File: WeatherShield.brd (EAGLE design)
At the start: 104.1 x 58.4 mm, 66 parts, among them J7 M023.5MM, J8 M023.5MM, Q1 BSS138, Q2 BSS138, U1 DS3231SN, U2 LT3652, U4 MPL3115A2LGA8, U5 HTU21D

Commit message: Power parts
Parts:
- removed J7, J8: M023.5MM, SparkFun-Connectors:SCREWTERMINAL-3.5MM-2
- removed L1: 68uH, SparkFun-Passives:CR75
- added L2: (no value), rcl:6000-XXXX-RC
- C3, C4: device SparkFun-Capacitors:EIA3528 -> FSEWeatherShield:EIA7343-20
- R21, R23, R8: device rcl:R0603 -> rcl:R0805
- U$3: value DEAN_CONNECTOR -> V_BATT
- moved R23 172.0 mm to (41.9, 67.3), turned to 180 degrees
- moved R21 164.7 mm to (41.9, 63.5), turned to 180 degrees
- moved R22 147.9 mm to (38.1, 55.9), turned to 180 degrees
- moved TP1 138.2 mm to (41.9, 49.5), turned to 180 degrees
- moved R10 126.4 mm to (41.9, 43.2), turned to 180 degrees
- moved R20 119.6 mm to (30.5, 43.2), turned to 180 degrees
- moved C9 113.4 mm to (43.2, 36.8), turned to 180 degrees
- moved U2 111.9 mm to (44.5, 30.5), turned to 180 degrees
- moved JP1 108.0 mm to (41.9, 27.9), turned to 180 degrees
- moved R8 108.0 mm to (39.4, 34.3), turned to 180 degrees
- moved JP2 106.8 mm to (45.7, 26.7), turned to 180 degrees
- moved C11 104.4 mm to (30.5, 35.6), turned to 90 degrees
- moved C2 102.9 mm to (39.4, 26.7), turned to 180 degrees
- moved R9 101.6 mm to (26.7, 33.0), turned to 270 degrees
- moved C10 100.6 mm to (36.8, 30.5), turned to 270 degrees
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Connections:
- net GND: no longer J8.2
- net N$14: no longer J7.2, J8.1
- net SENSE: now also L2.2; no longer L1.P$2
- net SFSASDF: no longer J7.1
- net SW: now also L2.1; no longer L1.P$1
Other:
- board size 104.1 x 58.4 mm -> 97.8 x 67.3 mm

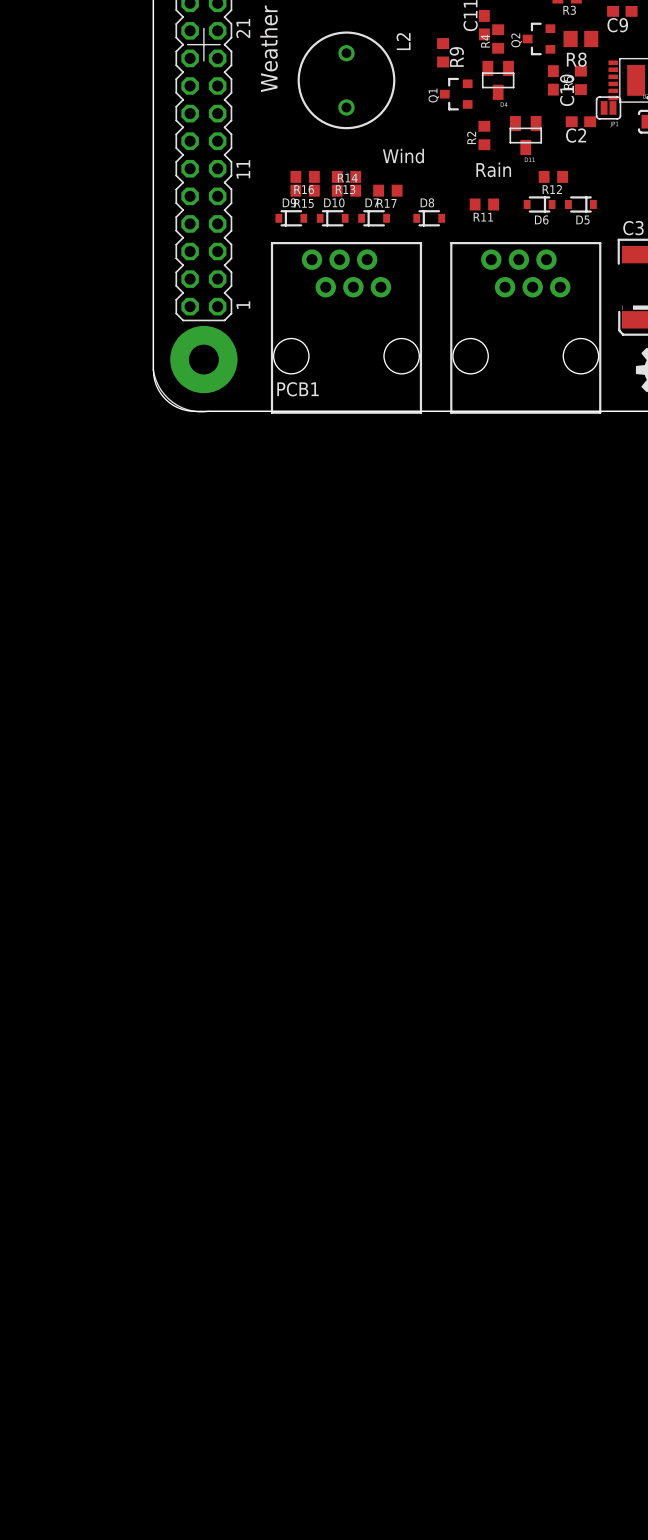
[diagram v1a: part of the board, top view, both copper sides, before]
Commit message: 5V supply done
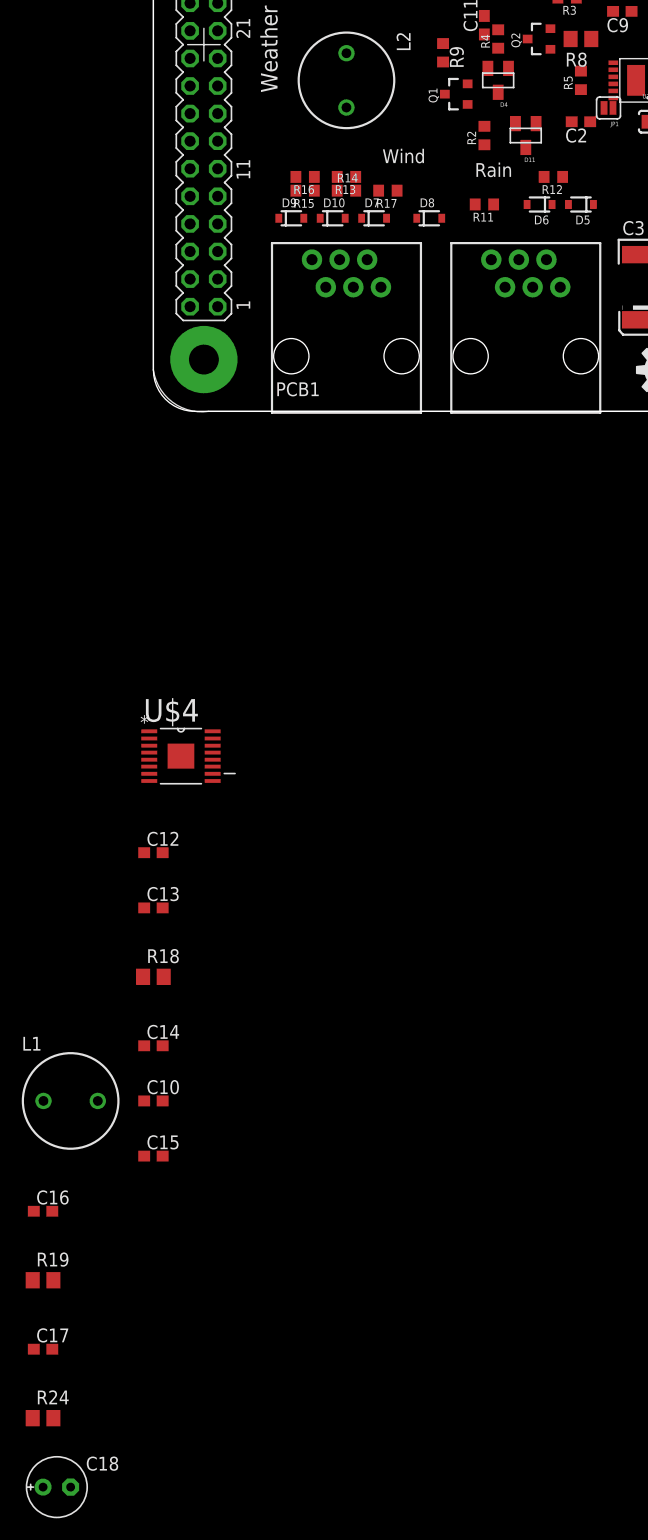
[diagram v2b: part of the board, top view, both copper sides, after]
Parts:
- added C12: 1uF, rcl:C0603
- added C13, C16: 4.7u, rcl:C0603
- added C14: 2.2uF, rcl:C0603
- added C15: 470nF, rcl:C0603
- added C17: 39pF, rcl:C0603
- added C18: 100uF, rcl:E2,5-6E
- added L1: 33uH, rcl:6000-XXXX-RC
- added R18: 0.2, rcl:R0805
- added R19: 1M, rcl:R0805
- added R24: 249k, rcl:R0805
- added U$4: LM43602, FSEWeatherShield:HTSSOP-16
- C10: value 1.0uF -> 1uF
- L2: value (none) -> 68uH
- moved C10 100.9 mm to (0.00, -63.5), turned to 0 degrees
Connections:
- new net +5V: C16.1, C17.1, C18.+, L1.2, R19.2, U$4.5
- new net N$17: C15.1, U$4.3
- new net N$21: R18.2, U$4.7
- new net N$22: C17.2, R19.1, R24.2, U$4.9
- new net N$23: C14.1, U$4.4
- new net N$24: C15.2, L1.1, U$4.1, U$4.2
- net GND: now also C12.2, C13.2, C14.2, C16.2, C18.-, R18.1, R24.1, U$4.10, U$4.15, U$4.16, U$4.17, U$4.6
- net V_BATT: now also C12.1, C13.1, U$4.12, U$4.13, U$4.14

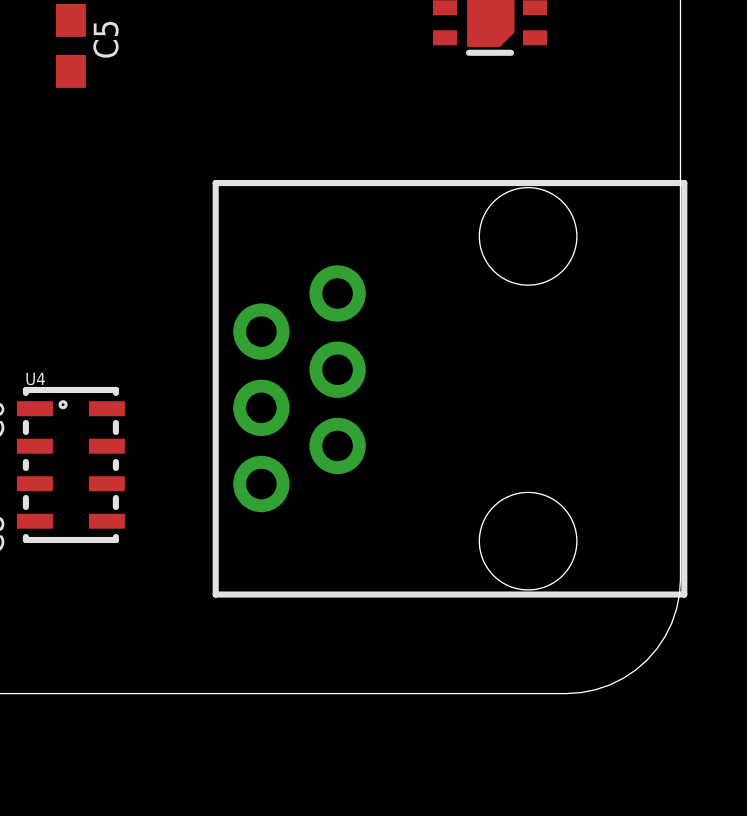
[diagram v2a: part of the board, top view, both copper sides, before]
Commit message: EagleCleanup.py added
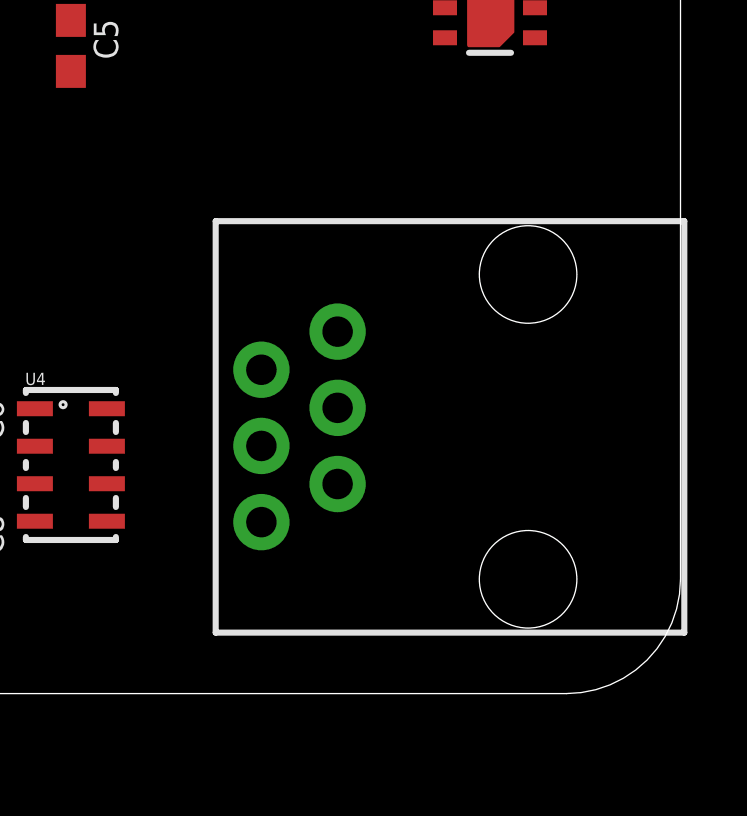
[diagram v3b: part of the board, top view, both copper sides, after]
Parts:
- moved JP9-DNP2 1.27 mm to (92.7, 35.6)
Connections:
- new net N$18: JP9-DNP1.6, JP9-DNP2.1
- new net N$19: JP9-DNP1.5, JP9-DNP2.2
- new net N$20: JP9-DNP1.4, JP9-DNP2.3
- new net N$25: JP9-DNP1.3, JP9-DNP2.4
- new net N$26: JP9-DNP1.2, JP9-DNP2.5
- new net N$27: JP9-DNP1.1, JP9-DNP2.6
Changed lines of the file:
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@@
 <element name="PCB1" library="FSE_Weather_Shield" package="RASPBERRY_PI_BPLUS_DIM" value="RASPBERRY_PI_B+/PI2_DIM" x="58.42" y="0" rot="R90"/>
 <element name="JP9-DNP1" library="SparkFun" package="RJ11-6" value="" x="44.45" y="62.23" rot="R180"/>
-<element name="JP9-DNP2" library="SparkFun" package="RJ11-6" value="" x="92.71" y="36.83" rot="R90"/>
+<element name="JP9-DNP2" library="SparkFun" package="RJ11-6" value="" x="92.71" y="35.56" rot="R90"/>
 <element name="R7" library="rcl" package="R0603" value="1K" x="53.34" y="58.42" rot="R180"/>
 <element name="D2" library="SparkFun" package="LED-0603" value="Blue" x="49.53" y="58.42" rot="R90"/>
@@
 <wire x1="-0.381" y1="-32.0802" x2="-5.12" y2="-63.5" width="0" layer="19" extent="1-1"/>
 </signal>
+<signal name="N$18">
+<contactref element="JP9-DNP1" pad="6"/>
+<contactref element="JP9-DNP2" pad="1"/>
+<wire x1="36.195" y1="55.88" x2="83.82" y2="37.465" width="0" layer="19" extent="1-1"/>
+</signal>
+<signal name="N$19">
+<contactref element="JP9-DNP1" pad="5"/>
+<contactref element="JP9-DNP2" pad="2"/>
+<wire x1="37.465" y1="53.34" x2="86.36" y2="38.735" width="0" layer="19" extent="1-1"/>
+</signal>
+<signal name="N$20">
+<contactref element="JP9-DNP1" pad="4"/>
+<contactref element="JP9-DNP2" pad="3"/>
+<wire x1="38.735" y1="55.88" x2="83.82" y2="40.005" width="0" layer="19" extent="1-1"/>
+</signal>
+<signal name="N$25">
+<contactref element="JP9-DNP1" pad="3"/>
+<contactref element="JP9-DNP2" pad="4"/>
+<wire x1="40.005" y1="53.34" x2="86.36" y2="41.275" width="0" layer="19" extent="1-1"/>
+</signal>
+<signal name="N$26">
+<contactref element="JP9-DNP1" pad="2"/>
+<contactref element="JP9-DNP2" pad="5"/>
+<wire x1="41.275" y1="55.88" x2="83.82" y2="42.545" width="0" layer="19" extent="1-1"/>
+</signal>
+<signal name="N$27">
+<contactref element="JP9-DNP1" pad="1"/>
+<contactref element="JP9-DNP2" pad="6"/>
+<wire x1="42.545" y1="53.34" x2="86.36" y2="43.815" width="0" layer="19" extent="1-1"/>
+</signal>
 </signals>

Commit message: Power parts
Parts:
- added D12: AirBoard status led, SparkFun:LED-0603
- added R25: 1K, rcl:R0603
- JP1: device SparkFun-Passives:SJ_2S -> jumper:JP1
- JP2: device SparkFun-Passives:SJ_2S-NO -> jumper:JP1
- moved C18 159.1 mm to (94.5, 21.8), turned to 90 degrees
- moved R24 150.0 mm to (88.1, 20.6), turned to 90 degrees
- moved C15 143.7 mm to (99.8, 34.8), turned to 90 degrees
- moved C17 141.0 mm to (81.8, 20.6), turned to 90 degrees
- moved L1 134.4 mm to (88.6, 30.2), turned to 90 degrees
- moved R19 132.1 mm to (75.4, 20.6), turned to 90 degrees
- moved C14 129.3 mm to (89.7, 34.8), turned to 90 degrees
- moved C16 123.1 mm to (69.1, 20.6), turned to 90 degrees
- moved R18 120.4 mm to (83.3, 34.8), turned to 90 degrees
- moved C13 111.4 mm to (77.0, 34.8), turned to 90 degrees
- moved C12 104.2 mm to (71.9, 34.8), turned to 90 degrees
- moved C10 97.5 mm to (43.2, 23.9), turned to 90 degrees
- moved U$4 95.9 mm to (77.2, 28.4), turned to 90 degrees
- moved LOGO1 47.9 mm to (72.4, 44.5)
- moved R8 43.7 mm to (69.1, 2.29)
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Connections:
- new net N$28: D12.A, R25.2
- new net STAT1: R25.1
- net GND: now also D12.C
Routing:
- added copper zone on layer 1, net GND
- added copper zone on layer 16, net GND
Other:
- board size 97.8 x 67.3 mm -> 100.3 x 67.3 mm

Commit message: routing
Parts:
- removed R18: 0.2, rcl:R0805
- added C19: 0.1uF, rcl:C1206
- C12: value 1uF -> 0.1uF; device rcl:C0603 -> rcl:C1206
- C13: device rcl:C0603 -> rcl:C1206
- C17: value 39pF -> 47pF
- L1: value 33uH -> 10uH
- moved R4 86.4 mm to (91.2, 2.03), turned to 0 degrees
- moved Q1 83.0 mm to (91.2, 4.57), turned to 270 degrees
- moved C18 81.9 mm to (15.2, 42.7), turned to 0 degrees
- moved R3 81.8 mm to (88.6, 4.57), turned to 270 degrees
- moved C15 78.2 mm to (21.8, 28.4), turned to 180 degrees
- moved R5 78.0 mm to (91.2, 8.38), turned to 0 degrees
- moved R23 76.0 mm to (82.8, 3.30)
- moved Q2 74.7 mm to (91.2, 10.9), turned to 270 degrees
- moved R2 73.3 mm to (88.6, 10.9), turned to 270 degrees
- moved L1 72.9 mm to (15.7, 32.3), turned to 180 degrees
- moved R21 70.7 mm to (82.5, 5.59)
- moved R24 66.5 mm to (26.7, 46.0)
- moved C14 65.0 mm to (24.9, 29.5), turned to 0 degrees
- moved C17 61.1 mm to (28.7, 50.8), turned to 180 degrees
- moved JP3 60.6 mm to (80.3, 0.76), turned to 0 degrees
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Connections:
- removed net 3V3: PCB1.1, PCB1.17
- removed net 5V0: PCB1.2, PCB1.4
- removed net N$18: JP9-DNP1.6, JP9-DNP2.1
- removed net N$19: JP9-DNP1.5, JP9-DNP2.2
- removed net N$20: JP9-DNP1.4, JP9-DNP2.3
- removed net N$21: R18.2, U$4.7
- removed net N$25: JP9-DNP1.3, JP9-DNP2.4
- removed net N$26: JP9-DNP1.2, JP9-DNP2.5
- removed net N$27: JP9-DNP1.1, JP9-DNP2.6
- net +5V: now also C19.1
- net 5V: now also PCB1.2, PCB1.4
- net GND: now also C19.2; no longer R18.1
- net VCC: now also PCB1.1, PCB1.17
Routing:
- net +5V: track 0.00 -> 46.9 mm, vias 0 -> 3
- net VCC: track 0.00 -> 37.6 mm, vias 0 -> 1
- net GND: track 0.00 -> 19.7 mm, vias 0 -> 9
- net N$6: track 0.00 -> 17.0 mm
- net WDIR: track 0.00 -> 11.4 mm
- net N$22: track 0.00 -> 9.12 mm
- net N$2: track 0.00 -> 8.44 mm
- net WSPEED: track 0.00 -> 8.08 mm
- net N$11: track 0.00 -> 7.88 mm
- net N$17: track 0.00 -> 7.46 mm
- net N$23: track 0.00 -> 6.82 mm
- net 5V: track 0.00 -> 6.03 mm
- net N$13: track 0.00 -> 5.50 mm
- net RAIN: track 0.00 -> 5.36 mm
- net N$12: track 0.00 -> 4.05 mm
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- added copper zone on layer 1, net +5V
- added copper zone on layer 1, net N$22
- added copper zone on layer 1, net N$24
- added copper zone on layer 1, net V_BATT

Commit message: routing...
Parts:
- moved C9 22.8 mm to (66.3, 31.5), turned to 270 degrees
- moved U2 15.5 mm to (83.5, 24.2), turned to 0 degrees
- moved R16 3.14 mm to (21.3, 17.0)
- moved R15 2.54 mm to (18.5, 17.0)
- moved Q1 0.05 mm to (91.2, 4.57)
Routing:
- net 5V: track 6.03 -> 46.7 mm
- net GND: track 19.7 -> 39.8 mm, vias 9 -> 12
- net N$13: track 5.50 -> 15.8 mm
- net N$11: track 7.88 -> 15.3 mm
- net +5V: track 46.9 -> 51.1 mm
- net WDIR: track 11.4 -> 13.3 mm

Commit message: Power parts
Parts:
- added C20, C21: 0.1uF, rcl:C0603
- added U$5: MCP3221A5T-E/OT, FSEWeatherShield:SOT95P270X145-5N
- JP10-DNP, JP9-DNP: device SparkFun:RJ11-6 -> FSEWeatherShield:RJ11-STECKER
- JP9-DNP1, JP9-DNP2: value (none) -> RJ11-BUCHSE; device SparkFun:RJ11-6 -> FSEWeatherShield:RJ11-STECKER
- R22: value 10k -> (none); device pot:S64Y -> pot:SM-42/43A
- moved R22 63.2 mm to (20.9, 32.3)
- moved U2 50.3 mm to (33.3, 25.6)
- moved C2 49.5 mm to (31.1, 36.0)
- moved C10 42.1 mm to (33.0, 36.1)
- moved C1 33.8 mm to (38.1, 39.9), turned to 0 degrees
- moved D4 32.6 mm to (37.4, 30.0)
- moved C15 32.0 mm to (18.4, 60.2), turned to 0 degrees
- moved C14 31.2 mm to (15.4, 59.2), turned to 180 degrees
- moved D11 29.0 mm to (41.5, 18.8)
- moved C16 26.8 mm to (14.9, 56.7), turned to 180 degrees
- moved L1 25.7 mm to (24.5, 56.4), turned to 0 degrees
- moved U1 23.7 mm to (38.2, 48.0), turned to 270 degrees
- moved C17 21.5 mm to (11.6, 37.9), turned to 0 degrees
- moved R19 19.3 mm to (11.6, 39.9), turned to 180 degrees
- moved R24 13.5 mm to (13.6, 42.7), turned to 270 degrees
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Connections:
- net 5V: now also C20.1, C21.1, U$5.1
- net GND: now also C20.2, C21.2, R22.1, U$5.2; no longer R22.A
- net SCL: now also U$5.5
- net SDA: now also U$5.4
- net SET: now also R22.2; no longer R22.S
- net VIN: now also R22.3; no longer R22.E
- net WDIR: now also U$5.3
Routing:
- net VCC: track 37.6 -> 0.00 mm, vias 1 -> 0
- net N$6: track 17.0 -> 0.00 mm
- net N$13: track 15.8 -> 0.00 mm
- net N$11: track 15.3 -> 0.00 mm
- net GND: track 39.8 -> 24.6 mm, vias 12 -> 10
- net N$2: track 8.59 -> 0.00 mm
- net N$1: track 4.05 -> 0.00 mm
- net N$4: track 3.43 -> 0.00 mm
- net N$12: track 3.94 -> 0.93 mm

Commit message: Power parts
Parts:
- removed JP1, JP2: (no value), jumper:JP1
- removed U$1: DEAN_CONNECTOR, FSE_Weather_Shield:DEAN_CONNECTOR
- moved R2 78.4 mm to (12.2, 28.1)
- moved Q2 78.0 mm to (15.1, 28.1)
- moved R5 77.5 mm to (15.5, 25.1)
- moved R3 74.6 mm to (18.4, 29.6)
- moved Q1 74.4 mm to (21.6, 30.7)
- moved R4 72.7 mm to (23.4, 28.3), turned to 90 degrees
- moved R23 61.3 mm to (29.5, 33.5), turned to 270 degrees
- moved R8 59.9 mm to (32.8, 33.5), turned to 270 degrees
- moved R21 58.5 mm to (31.1, 33.5), turned to 270 degrees
- moved D1 50.9 mm to (46.0, 5.08), turned to 180 degrees
- moved D3 48.7 mm to (43.3, 5.08), turned to 180 degrees
- moved R1 48.6 mm to (46.0, 7.87), turned to 270 degrees
- moved JP3 47.2 mm to (46.2, 33.5), turned to 90 degrees
- moved R6 46.6 mm to (43.3, 7.87), turned to 270 degrees
- moved L2 46.1 mm to (38.9, 35.6), turned to 180 degrees
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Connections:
- removed net N$14: JP1.1, U$1.2, U$2.1
- removed net SFSASDF: JP2.1, U$1.1
- net 5V: now also JP9-DNP1.1, JP9-DNP2.1
- net GND: now also JP9-DNP1.5, JP9-DNP1.6, JP9-DNP2.5, JP9-DNP2.6
- net SCL: now also JP9-DNP1.4, JP9-DNP2.4
- net SDA: now also JP9-DNP1.3, JP9-DNP2.3
- net VCC: now also JP9-DNP1.2, JP9-DNP2.2
- net VIN: now also U$2.1; no longer JP1.2, JP2.2
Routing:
- net VCC: track 0.00 -> 98.2 mm, vias 0 -> 1
- net 5V: track 46.7 -> 136.6 mm, vias 0 -> 1
- net V_BATT: track 0.00 -> 70.9 mm, vias 0 -> 3
- net SCL: track 0.00 -> 64.1 mm, vias 0 -> 3
- net SDA: track 0.00 -> 63.2 mm, vias 0 -> 3
- net N$6: track 0.00 -> 31.0 mm, vias 0 -> 1
- net GND: track 24.6 -> 55.2 mm, vias 10 -> 13
- net N$16: track 0.00 -> 27.2 mm, vias 0 -> 2
- net VIN: track 0.00 -> 26.1 mm
- net !CHRG: track 0.00 -> 21.6 mm, vias 0 -> 2
- net !FAULT: track 0.00 -> 20.8 mm, vias 0 -> 2
- net N$2: track 0.00 -> 16.1 mm
- net SENSE: track 0.00 -> 15.1 mm, vias 0 -> 1
- net WDIR: track 13.3 -> 26.8 mm, vias 0 -> 2
- net N$11: track 0.00 -> 10.8 mm
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- added copper zone on layer 1, net N$16
- added copper zone on layer 1, net SENSE
- added copper zone on layer 1, net SW
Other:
- board size 100.3 x 67.3 mm -> 90.3 x 67.3 mm
- board text added: "FSE Weather Shield V1"
- board text removed: "Weather Shield V1"
